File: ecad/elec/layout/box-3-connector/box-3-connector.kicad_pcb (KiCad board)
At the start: 2 copper layers, 225.7 x 100.8 mm, 0 parts

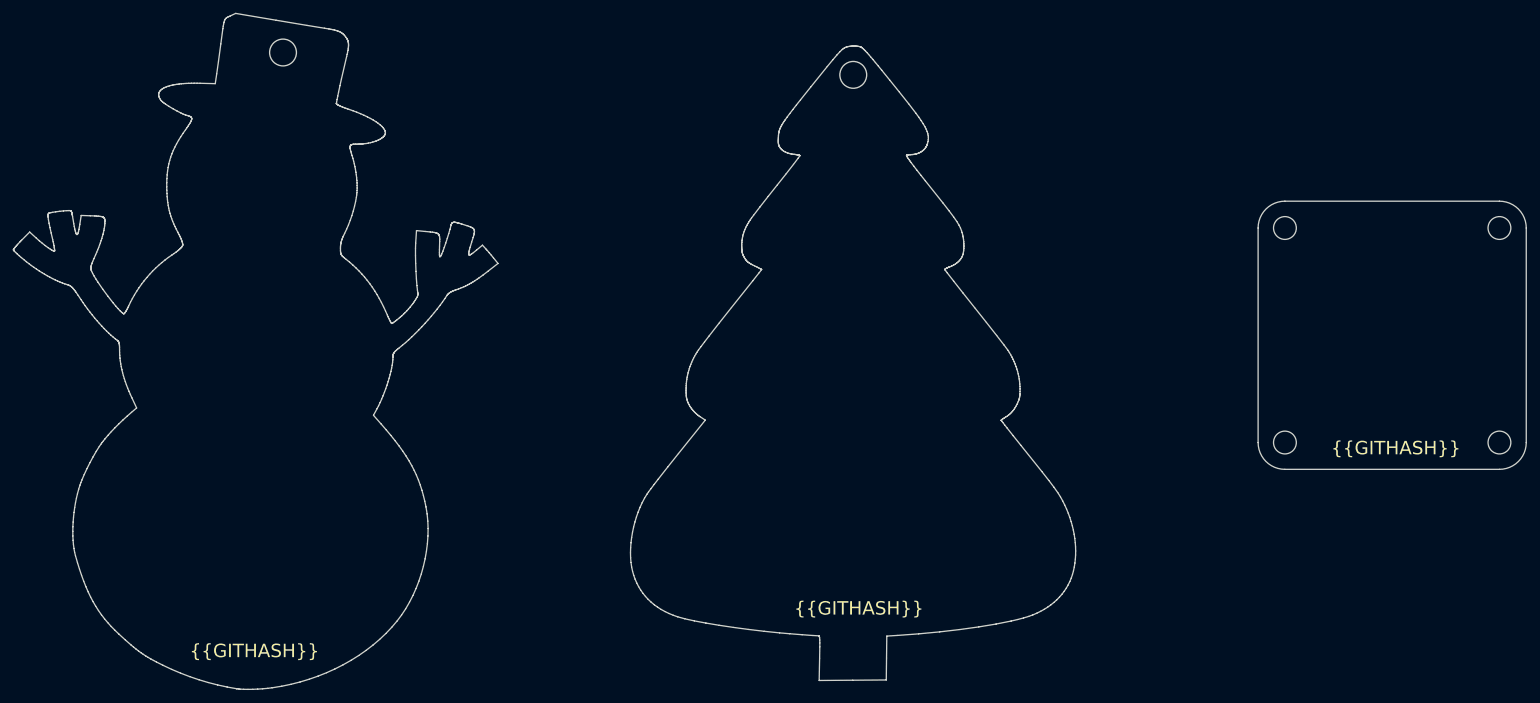
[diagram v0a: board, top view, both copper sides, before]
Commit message: remove and ignore kicad_prl files
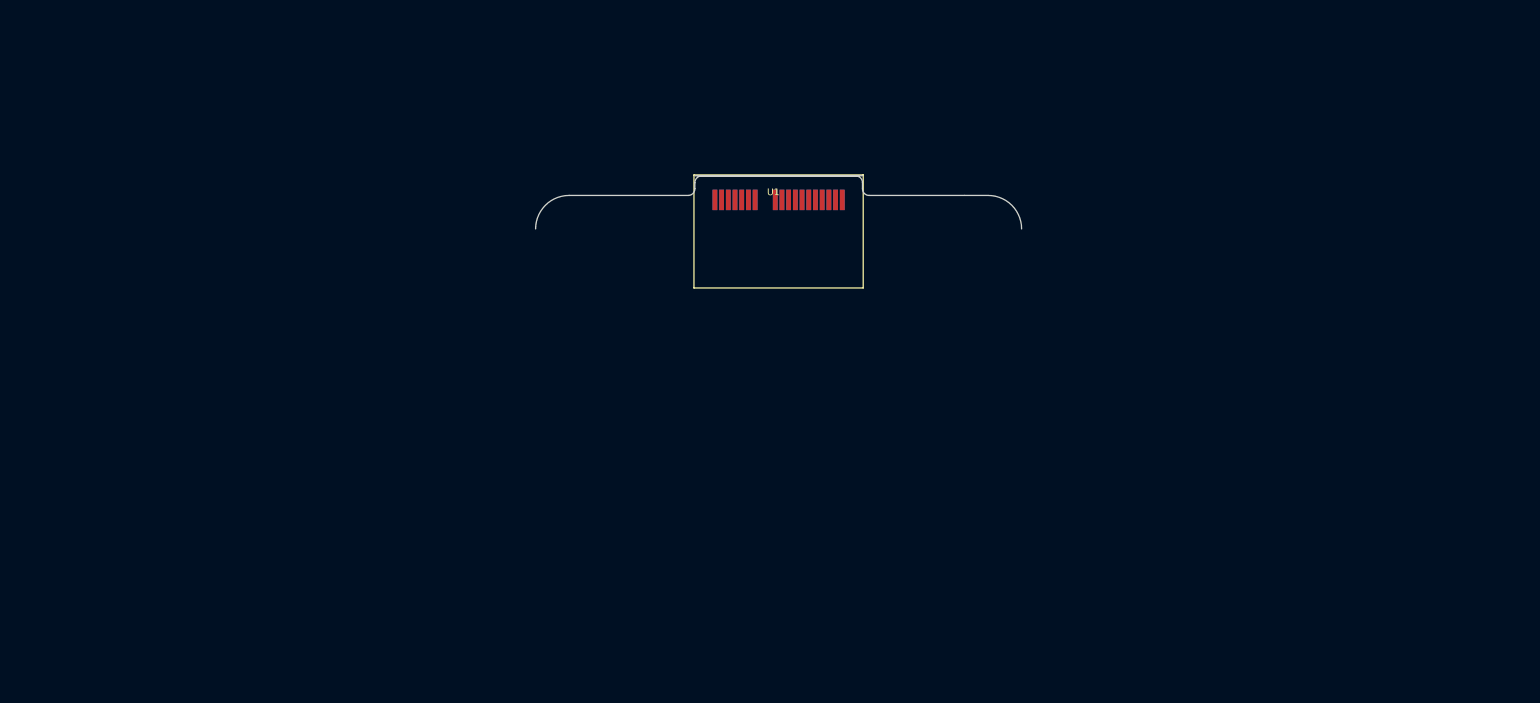
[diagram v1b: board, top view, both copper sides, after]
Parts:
- added U1: , lib:BOX_3_EMU, F.Cu at (149.3, 76.9)
- added U2: , lib:CONN_5-1734857-1_TEC, F.Cu at (150.1, 77.6)
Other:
- board size 225.7 x 100.8 mm -> 72.5 x 7.9 mm
- board text removed: "{{GITHASH}}"
